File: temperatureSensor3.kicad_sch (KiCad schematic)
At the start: 3 parts, among them J2 Conn_01x03_Pin

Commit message: first draft
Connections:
- net tempSensor1_OUT renamed tempSensor3_OUT
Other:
- note added: "Temperature Sensor 3"
- note removed: "Temperature Sensor 1"

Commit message: revision
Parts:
- added TP3: TestPoint, TestPoint:TestPoint_THTPad_D2.0mm_Drill1.0mm, symbol Connector:TestPoint
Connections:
- net tempSensor3_OUT: now also TP3.1
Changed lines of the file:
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@@
+    )
+  )
+  (symbol (lib_id "Connector:TestPoint") (at 114.3 60.96 0) (unit 1)
+    (in_bom yes) (on_board yes) (dnp no) (fields_autoplaced)
+    (property "Reference" "TP3" (at 116.84 56.388 0)
+      (effects (font (size 1.27 1.27)) (justify left))
+    )
+    (property "Value" "TestPoint" (at 116.84 58.928 0)
+      (effects (font (size 1.27 1.27)) (justify left))
+    )
+    (property "Footprint" "TestPoint:TestPoint_THTPad_D2.0mm_Drill1.0mm" (at 119.38 60.96 0)
+      (effects (font (size 1.27 1.27)) hide)
+    )
+    (property "Datasheet" "~" (at 119.38 60.96 0)
+      (effects (font (size 1.27 1.27)) hide)
+    )
+    (pin "1")
+    (instances
+      (project "Telemetry-Peripheral-SOM-Daughterboard-IMU"
+        (path "/637f68f0-cb9c-412a-8573-5d8e7ef6d8a2/5542d029-5813-4503-91aa-e34e1416dbcf"
+          (reference "TP3") (unit 1)
+        )
+      )
     )
   )

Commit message: Integrated changes made by BPS
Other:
- moved on the sheet: C7, C8, J2, TP3

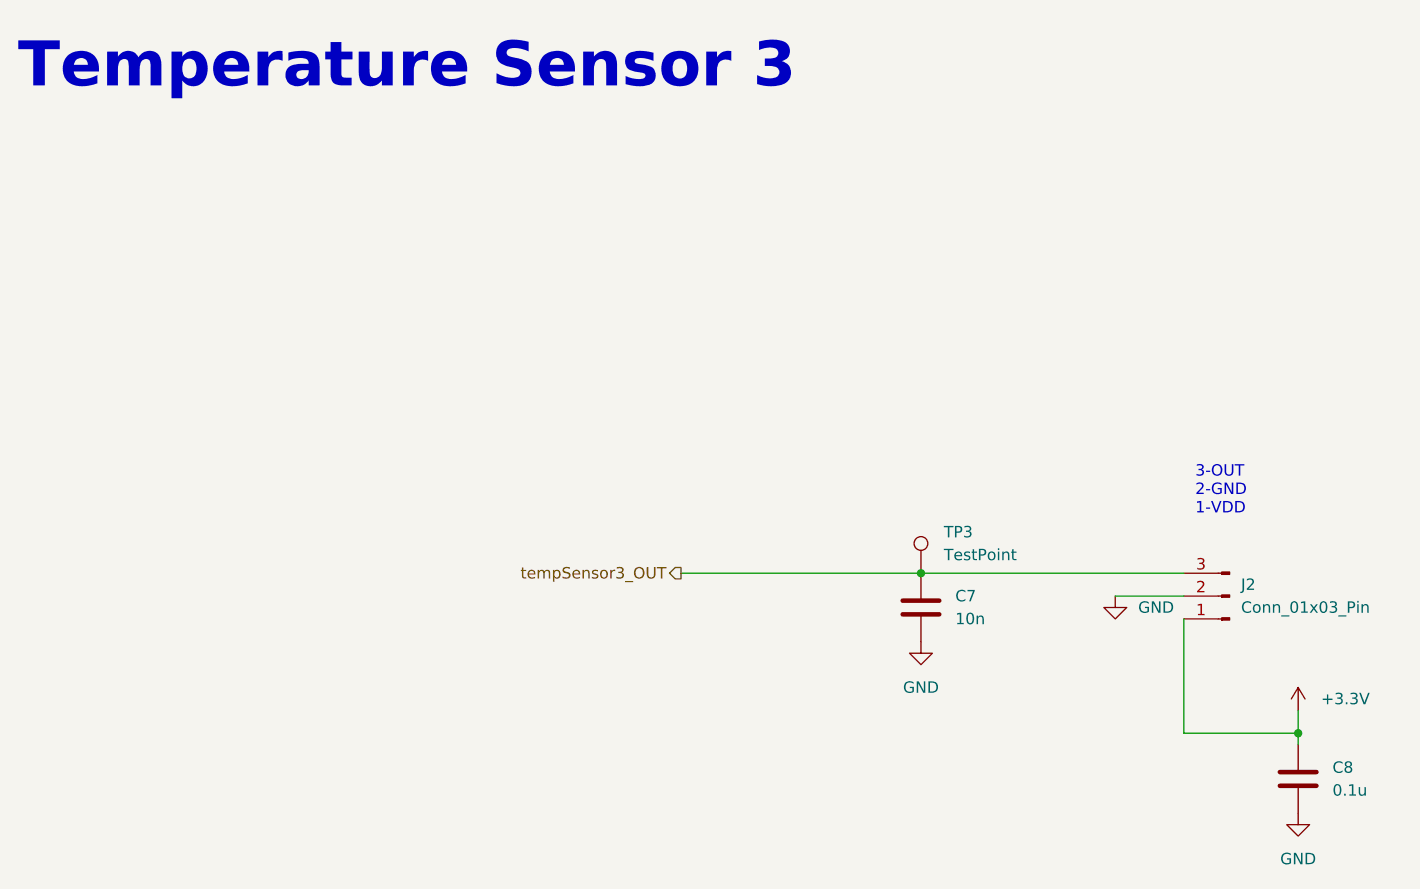
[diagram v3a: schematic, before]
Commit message: added protective circuitry for temp sensors, made name changes for IMU
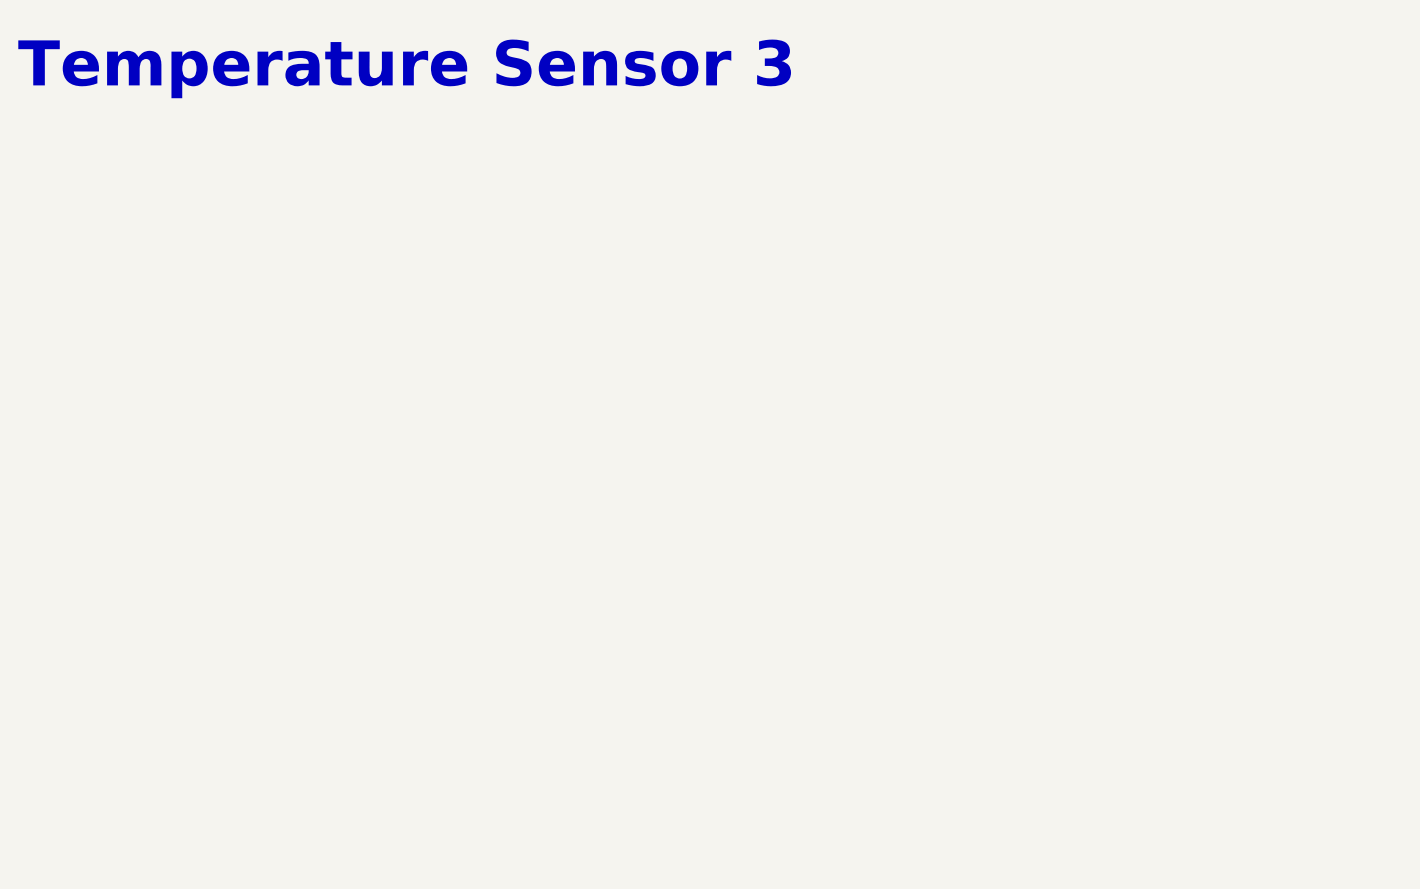
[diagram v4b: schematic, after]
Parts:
- removed C7: 10n, Capacitor_SMD:C_0805_2012Metric, symbol Device:C
- removed C8: 0.1u, Capacitor_SMD:C_0805_2012Metric, symbol Device:C
- removed J2: Conn_01x03_Pin, UTSVT_Connectors:Molex_MicroFit3.0_1x3xP3.00mm_PolarizingPeg_Vertical, symbol Connector:Conn_01x03_Pin
- removed TP3: TestPoint, TestPoint:TestPoint_THTPad_D2.0mm_Drill1.0mm, symbol Connector:TestPoint
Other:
- note removed: "3-OUT 2-GND 1-VDD"
